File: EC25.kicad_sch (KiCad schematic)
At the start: 23 parts, among them J4 1775862-2, Q2 AO3401A, SW2 SW_SPDT, U1 LM29300T-3.3

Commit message: mostly done except for RTL8305 power stuff
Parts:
- removed R19, R20, R21: 0, Resistor_SMD:R_0402_1005Metric, symbol Device:R
- added LED2: KT-0805G, LED_SMD:LED_0805_2012Metric, symbol LTELink:GREEN LED
- added R5: 510, Resistor_SMD:R_0402_1005Metric, symbol Device:R
- C40, LED7, Q2, R1, R17, R18: now not fitted; now left out of the parts list
- D1, SIM1: now left out of the parts list
- J4: value 1775862-2 -> 1759547-1; footprint LTELink:TE_1775862-2 -> LTELink:TE_1759547-1; now left out of the parts list
- R16: value 820 -> 1k
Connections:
- net +3.3V: now also R5.2
- net GND: now also LED2.2
- net USIM_CLK: now also SIM1.3 (CLK)
- net USIM_DATA: now also R2.2, SIM1.7 (I/O)
- net USIM_RST: now also SIM1.2 (RST)
- new net: LED2.1, R5.1
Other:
- note added: "3.3V Power"

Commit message: replaced ferrites with 0 omh resitors, finalized standoff solution
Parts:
- added C13: 10u, Capacitor_SMD:C_0603_1608Metric, symbol Device:C_Polarized
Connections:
- net +5V: now also C13.1
- net GND: now also C13.2
- no-connect marks 13 -> 14
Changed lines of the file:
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@@
 	)
 	(rectangle
-		(start 229.87 69.85)
+		(start 220.98 69.85)
 		(end 273.05 104.14)
 		(stroke
@@
 	)
 	(junction
+		(at 229.87 85.09)
+		(diameter 0)
+		(color 0 0 0 0)
+	)
+	(junction
 		(at 104.14 135.89)
 		(diameter 0)
@@
 	)
 	(junction
+		(at 229.87 77.47)
+		(diameter 0)
+		(color 0 0 0 0)
+	)
+	(junction
 		(at 66.04 44.45)
 		(diameter 0)
@@
 	)
 	(no_connect
+		(at 224.79 127)
+	)
+	(no_connect
 		(at 48.26 177.8)
 	)
@@
 	(wire
 		(pts
+			(xy 233.68 85.09) (xy 233.68 82.55)
+		)
+		(stroke
+			(width 0)
+			(type default)
+		)
+	)
+	(wire
+		(pts
 			(xy 158.75 104.14) (xy 171.45 104.14)
 		)
@@
 	(wire
 		(pts
+			(xy 229.87 85.09) (xy 233.68 85.09)
+		)
+		(stroke
+			(width 0)
+			(type default)
+		)
+	)
+	(wire
+		(pts
 			(xy 91.44 30.48) (xy 91.44 31.75)
 		)
@@
 	(wire
 		(pts
+			(xy 233.68 77.47) (xy 229.87 77.47)
+		)
+		(stroke
+			(width 0)
+			(type default)
+		)
+	)
+	(wire
+		(pts
 			(xy 109.22 45.72) (xy 109.22 39.37)
 		)
@@
 	(wire
 		(pts
+			(xy 233.68 80.01) (xy 233.68 77.47)
+		)
+		(stroke
+			(width 0)
+			(type default)
+		)
+	)
+	(wire
+		(pts
 			(xy 106.68 162.56) (xy 104.14 162.56)
 		)
@@
 	(symbol
 		(lib_id "power:GND")
-		(at 233.68 82.55 0)
+		(at 229.87 85.09 0)
 		(unit 1)
 		(exclude_from_sim no)
@@
 		(dnp no)
 		(property "Reference" "#PWR069"
-			(at 233.68 88.9 0)
+			(at 229.87 91.44 0)
 			(effects
 				(font
@@
 		)
 		(property "Value" "GND"
-			(at 233.68 86.36 0)
+			(at 229.87 88.9 0)
 			(effects
 				(font
@@
 		)
 		(property "Footprint" ""
-			(at 233.68 82.55 0)
+			(at 229.87 85.09 0)
 			(effects
 				(font
@@
 		)
 		(property "Datasheet" ""
-			(at 233.68 82.55 0)
+			(at 229.87 85.09 0)
 			(effects
 				(font
@@
 		)
 		(property "Description" "Power symbol creates a global label with name \"GND\" , ground"
-			(at 233.68 82.55 0)
+			(at 229.87 85.09 0)
 			(effects
 				(font
@@
 	)
 	(symbol
+		(lib_id "Device:C_Polarized")
+		(at 229.87 81.28 0)
+		(unit 1)
+		(exclude_from_sim no)
+		(in_bom yes)
+		(on_board yes)
+		(dnp no)
+		(property "Reference" "C13"
+			(at 222.504 80.01 0)
+			(effects
+				(font
+					(size 1.27 1.27)
+				)
+				(justify left)
+			)
+		)
+		(property "Value" "10u"
+			(at 222.504 82.55 0)
+			(effects
+				(font
+					(size 1.27 1.27)
+				)
+				(justify left)
+			)
+		)
+		(property "Footprint" "Capacitor_SMD:C_0603_1608Metric"
+			(at 230.8352 85.09 0)
+			(effects
+				(font
+					(size 1.27 1.27)
+				)
+				(hide yes)
+			)
+		)
+		(property "Datasheet" "~"
+			(at 229.87 81.28 0)
+			(effects
+				(font
+					(size 1.27 1.27)
+				)
+				(hide yes)
+			)
+		)
+		(property "Description" "Polarized capacitor"
+			(at 229.87 81.28 0)
+			(effects
+				(font
+					(size 1.27 1.27)
+				)
+				(hide yes)
+			)
+		)
+		(property "Part Number" "CL10A106KP8NNNC"
+			(at 229.87 81.28 0)
+			(effects
+				(font
+					(size 1.27 1.27)
+				)
+				(hide yes)
+			)
+		)
+		(pin "2"
+		)
+		(pin "1"
+		)
+		(instances
+			(project "LTELink"
+				(path "/ebd96e19-6f65-4022-a6da-be26c0716f8e/b24baf21-5816-49e9-9ae3-74bfac20cf13"
+					(reference "C13")
+					(unit 1)
+				)
+			)
+		)
+	)
+	(symbol
 		(lib_id "Device:R")
 		(at 154.94 123.19 90)
@@
 	(symbol
 		(lib_id "power:+5V")
-		(at 233.68 80.01 0)
+		(at 229.87 77.47 0)
 		(unit 1)
 		(exclude_from_sim no)
@@
 		(fields_autoplaced yes)
 		(property "Reference" "#PWR068"
-			(at 233.68 83.82 0)
+			(at 229.87 81.28 0)
 			(effects
 				(font
@@
 		)
 		(property "Value" "+5V"
-			(at 233.68 74.93 0)
+			(at 229.87 72.39 0)
 			(effects
 				(font
@@
 		)
 		(property "Footprint" ""
-			(at 233.68 80.01 0)
+			(at 229.87 77.47 0)
 			(effects
 				(font
@@
 		)
 		(property "Datasheet" ""
-			(at 233.68 80.01 0)
+			(at 229.87 77.47 0)
 			(effects
 				(font
@@
 		)
 		(property "Description" "Power symbol creates a global label with name \"+5V\""
-			(at 233.68 80.01 0)
+			(at 229.87 77.47 0)
 			(effects
 				(font

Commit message: finalized board for fabrication
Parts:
- C13, C9: LCSC Part # (none) -> C96446
- C2: LCSC Part # (none) -> C15525
- C3, C4, C5: LCSC Part # (none) -> C1562
- LED2: LCSC Part # (none) -> C2297
- LED6: LCSC Part # (none) -> C2290
- R15: LCSC Part # (none) -> C25794
- R16: LCSC Part # (none) -> C11702
- R2: LCSC Part # (none) -> C25756
- R5: LCSC Part # (none) -> C25123
- U1: now not fitted

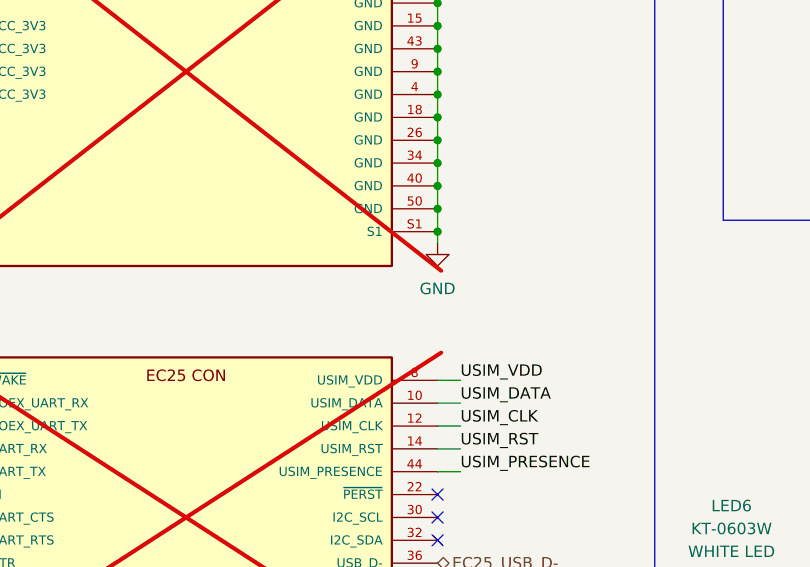
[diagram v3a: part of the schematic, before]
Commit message: fix incorrect footprint orientation and breakout uarts
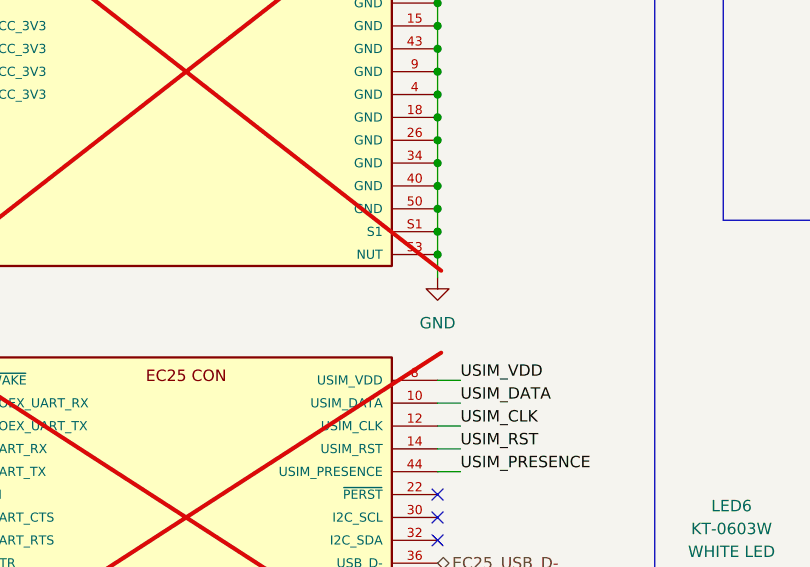
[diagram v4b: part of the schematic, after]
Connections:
- net GND: now also J4.53 (NUT)
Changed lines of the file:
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@@
 	)
 	(junction
+		(at 104.14 138.43)
+		(diameter 0)
+		(color 0 0 0 0)
+	)
+	(junction
 		(at 104.14 135.89)
 		(diameter 0)
@@
 	(wire
 		(pts
-			(xy 104.14 137.16) (xy 104.14 135.89)
+			(xy 104.14 135.89) (xy 104.14 138.43)
 		)
 		(stroke
@@
 	(wire
 		(pts
+			(xy 104.14 138.43) (xy 104.14 140.97)
+		)
+		(stroke
+			(width 0)
+			(type default)
+		)
+	)
+	(wire
+		(pts
 			(xy 106.68 160.02) (xy 104.14 160.02)
 		)
@@
 			)
 		)
-		(property "Datasheet" ""
+		(property "Datasheet" "https://jlcpcb.com/api/file/downloadByFileSystemAccessId/8588904760061120512"
 			(at 76.2 184.15 0)
 			(effects
@@
 			)
 		)
-		(property "Datasheet" ""
+		(property "Datasheet" "https://jlcpcb.com/api/file/downloadByFileSystemAccessId/8588904760061120512"
 			(at 76.2 104.14 0)
 			(effects
@@
 		(pin "S1"
 		)
+		(pin "53"
+		)
 		(instances
 			(project ""
@@
 	(symbol
 		(lib_id "power:GND")
-		(at 104.14 137.16 0)
+		(at 104.14 140.97 0)
 		(unit 1)
 		(exclude_from_sim no)
@@
 		(fields_autoplaced yes)
 		(property "Reference" "#PWR12"
-			(at 104.14 143.51 0)
+			(at 104.14 147.32 0)
 			(effects
 				(font
@@
 		)
 		(property "Value" "GND"
-			(at 104.14 142.24 0)
+			(at 104.14 146.05 0)
 			(effects
 				(font
@@
 		)
 		(property "Footprint" ""
-			(at 104.14 137.16 0)
+			(at 104.14 140.97 0)
 			(effects
 				(font
@@
 		)
 		(property "Datasheet" ""
-			(at 104.14 137.16 0)
+			(at 104.14 140.97 0)
 			(effects
 				(font
@@
 		)
 		(property "Description" "Power symbol creates a global label with name \"GND\" , ground"
-			(at 104.14 137.16 0)
+			(at 104.14 140.97 0)
 			(effects
 				(font
